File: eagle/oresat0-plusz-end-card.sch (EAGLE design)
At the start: 42 parts, among them J1 Harwin M55-7101242R, J10 R107064070_CONTACT, J11 R107064070_CONTACT, J12 R107064070_CONTACT, J13 R107064070_CONTACT, J14 R107064070_CONTACT, J15 R107064070_CONTACT, J16 R107064070_CONTACT, J2 Harwin M55-7101242R, J3 Harwin M55-7101242R, J4 Harwin M55-7101242R, J6 J-SAMTEC-TFM-120-X1-XXX-D-RA, J7 R107064070_CONTACT, J8 R107064070_CONTACT, J9 R107064070_CONTACT, U1 QCN-19+, U2 QCN-19+, U3 QCN-19+

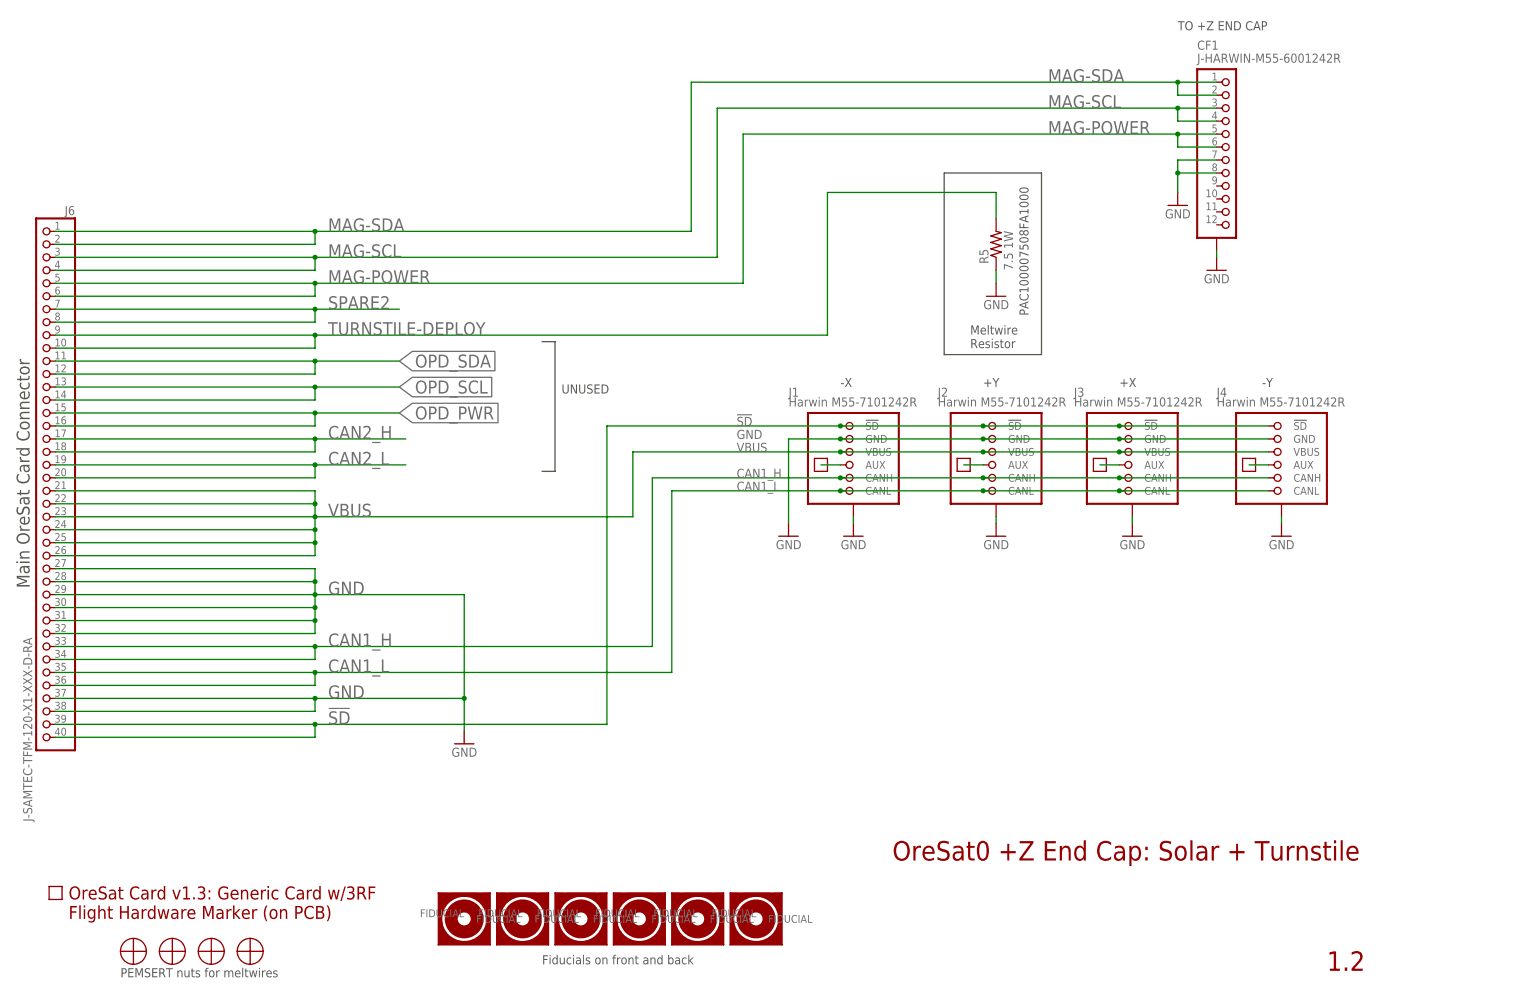
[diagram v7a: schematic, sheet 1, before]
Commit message: v2.0 card, mezzanine, and BOM for v2.0. Moved UHF hybrids to avoid melt wire resistor leads. Updated BOM to reflect new v2.0 design.
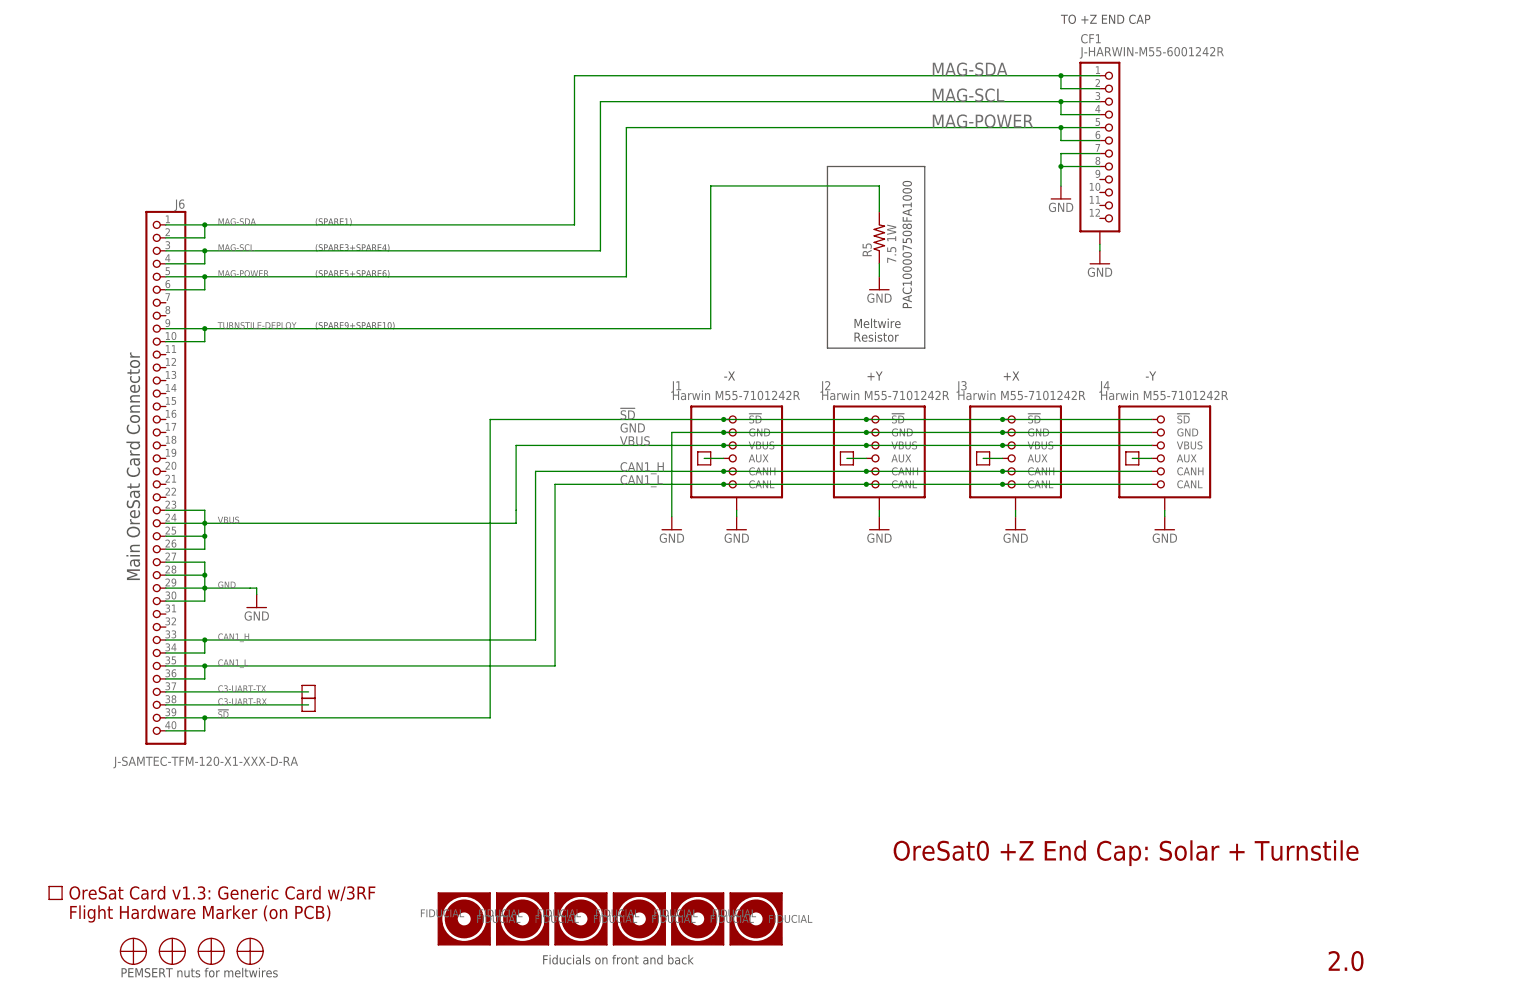
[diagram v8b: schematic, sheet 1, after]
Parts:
- added TP5, TP6: TEST-POINT-LARGE-SQUARE, oresat-misc:TEST-POINT-LARGE-SQUARE
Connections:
- removed net CAN2_H: J6.17, J6.18
- removed net CAN2_L: J6.19, J6.20
- removed net OPD_PWR: J6.15, J6.16
- removed net OPD_SCL: J6.13, J6.14
- removed net OPD_SDA: J6.11, J6.12
- removed net SPARE2: J6.7, J6.8
- new net C3-UART-RX: J6.38, TP5.1
- new net C3-UART-TX: J6.37, TP6.1
- net GND: no longer J6.31, J6.32, J6.37, J6.38
- net VBUS: no longer J6.21, J6.22
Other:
- note added: "(SPARE1)"
- note added: "(SPARE3+SPARE4)"
- note added: "(SPARE5+SPARE6)"
- note added: "(SPARE9+SPARE10)"
- note added: "1.265 GHz"
- note added: "2.0"
- note added: "4x L Band Elements (through holes)"
- note added: "4x L1 elements (through holes)"
- note added: "L Band Feed System (1.265 GHz)"
- note added: "L1 BAND Feed System (1.575 GHz)"
- note added: "UHF Feed System (436.5 MHz)"
- note removed: "1.2"
- note removed: "L Band Feed System"
- note removed: "L1 BAND Feed System"
- note removed: "UHF Feed System"
- note removed: "UNUSED"
- moved on the sheet: CF1, J1, J2, J3, J4, J6, R5
